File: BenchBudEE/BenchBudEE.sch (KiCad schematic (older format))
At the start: 0 parts

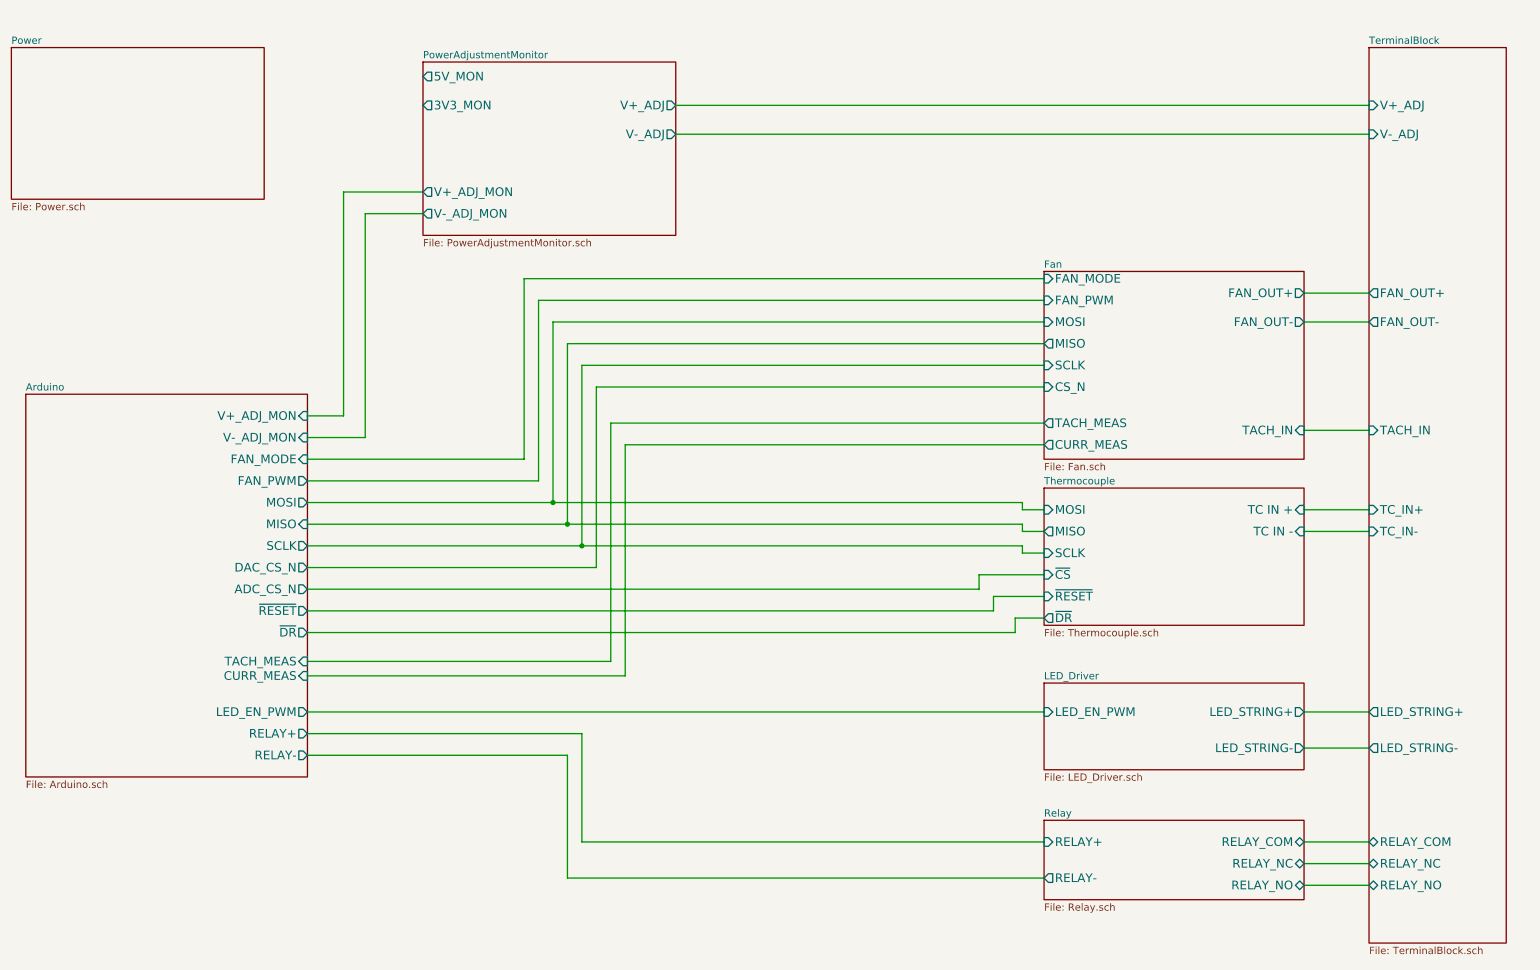
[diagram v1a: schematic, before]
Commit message: Associating the current/fan driver module components.
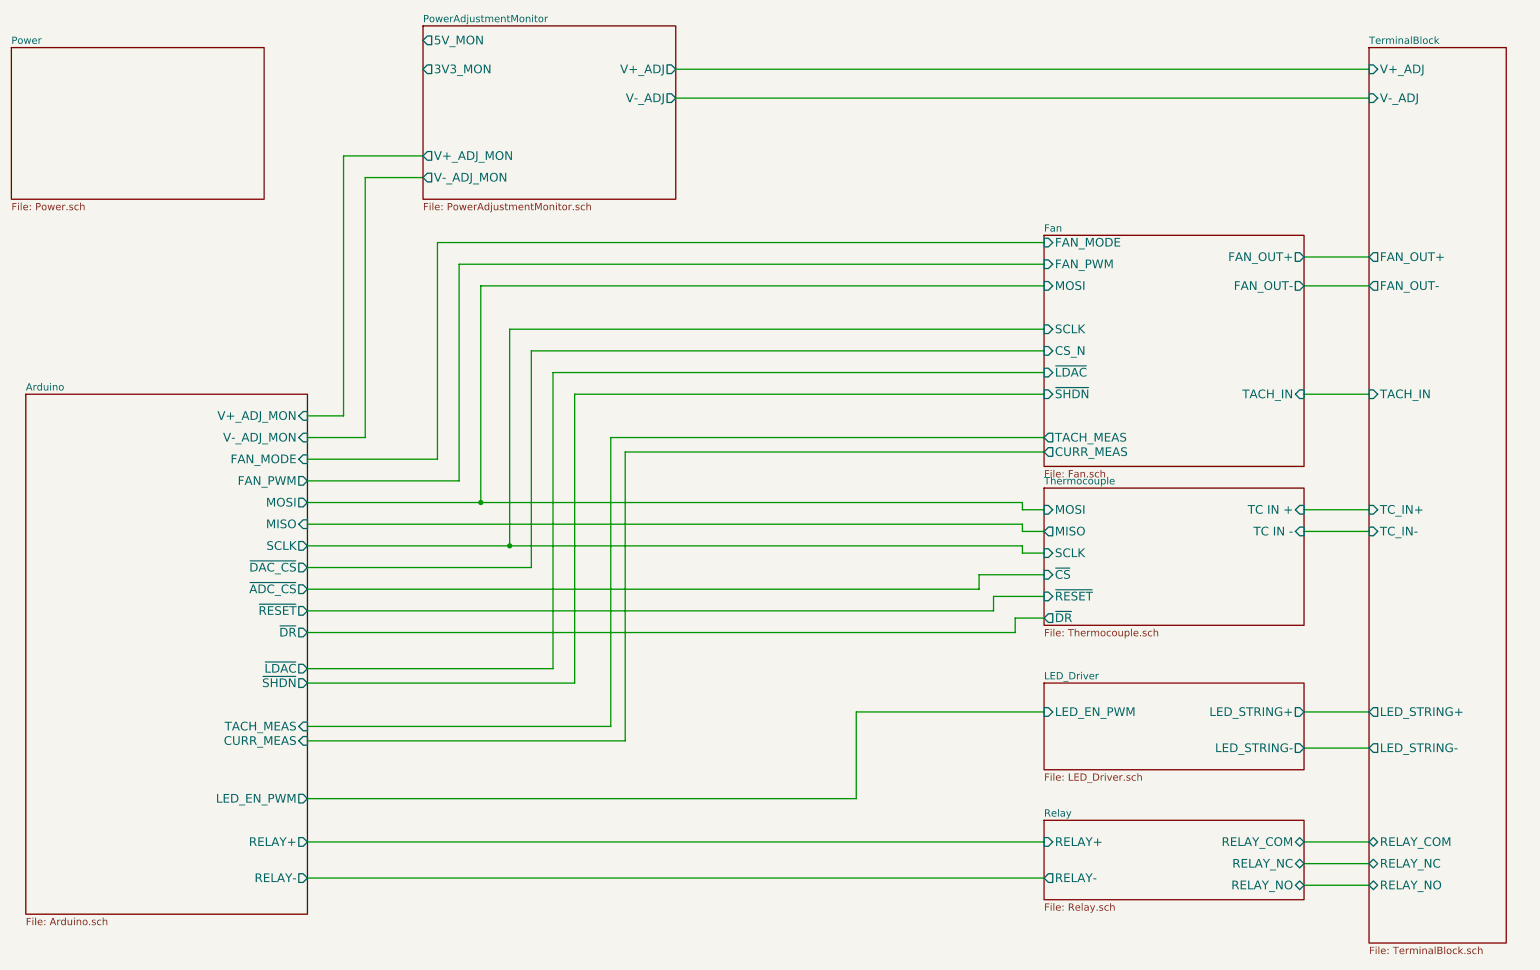
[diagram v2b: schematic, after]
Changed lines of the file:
@@
 $EndSheet
 $Sheet
-S 3550 850  1750 1200
+S 3550 600  1750 1200
 U 52F627C8
 F0 "PowerAdjustmentMonitor" 50
 F1 "PowerAdjustmentMonitor.sch" 50
-F2 "V+_ADJ" O R 5300 1150 60
-F3 "V-_ADJ" O R 5300 1350 60
-F4 "3V3_MON" O L 3550 1150 60
-F5 "5V_MON" O L 3550 950 60
-F6 "V+_ADJ_MON" O L 3550 1750 60
-F7 "V-_ADJ_MON" O L 3550 1900 60
-$EndSheet
-$Sheet
-S 7850 2300 1800 1300
+F2 "V+_ADJ" O R 5300 900 60
+F3 "V-_ADJ" O R 5300 1100 60
+F4 "3V3_MON" O L 3550 900 60
+F5 "5V_MON" O L 3550 700 60
+F6 "V+_ADJ_MON" O L 3550 1500 60
+F7 "V-_ADJ_MON" O L 3550 1650 60
+$EndSheet
+$Sheet
+S 7850 2050 1800 1600
 U 52EC4E13
 F0 "Fan" 50
 F1 "Fan.sch" 50
-F2 "MOSI" I L 7850 2650 60
-F3 "MISO" O L 7850 2800 60
-F4 "CS_N" I L 7850 3100 60
-F5 "SCLK" I L 7850 2950 60
-F6 "FAN_OUT+" O R 9650 2450 60
-F7 "TACH_IN" I R 9650 3400 60
-F8 "TACH_MEAS" O L 7850 3350 60
-F9 "CURR_MEAS" O L 7850 3500 60
-F10 "FAN_OUT-" O R 9650 2650 60
-F11 "FAN_PWM" I L 7850 2500 60
-F12 "FAN_MODE" I L 7850 2350 60
-$EndSheet
-Wire Wire Line
-	10100 1150 5300 1150
-Wire Wire Line
-	10100 1350 5300 1350
+F2 "MOSI" I L 7850 2400 60
+F3 "CS_N" I L 7850 2850 60
+F4 "SCLK" I L 7850 2700 60
+F5 "FAN_OUT+" O R 9650 2200 60
+F6 "TACH_IN" I R 9650 3150 60
+F7 "TACH_MEAS" O L 7850 3450 60
+F8 "CURR_MEAS" O L 7850 3550 60
+F9 "FAN_OUT-" O R 9650 2400 60
+F10 "FAN_PWM" I L 7850 2250 60
+F11 "FAN_MODE" I L 7850 2100 60
+F12 "~LDAC" I L 7850 3000 60
+F13 "~SHDN" I L 7850 3150 60
+$EndSheet
+Wire Wire Line
+	10100 900  5300 900
+Wire Wire Line
+	10100 1100 5300 1100
 $Sheet
 S 10100 750  950  6200
@@
 F0 "TerminalBlock" 50
 F1 "TerminalBlock.sch" 50
-F2 "V+_ADJ" I L 10100 1150 60
-F3 "V-_ADJ" I L 10100 1350 60
-F4 "FAN_OUT+" O L 10100 2450 60
-F5 "FAN_OUT-" O L 10100 2650 60
-F6 "TACH_IN" I L 10100 3400 60
+F2 "V+_ADJ" I L 10100 900 60
+F3 "V-_ADJ" I L 10100 1100 60
+F4 "FAN_OUT+" O L 10100 2200 60
+F5 "FAN_OUT-" O L 10100 2400 60
+F6 "TACH_IN" I L 10100 3150 60
 F7 "LED_STRING+" O L 10100 5350 60
 F8 "LED_STRING-" O L 10100 5600 60
@@
 $EndSheet
 Wire Wire Line
-	9650 2450 10100 2450
-Wire Wire Line
-	9650 2650 10100 2650
-Wire Wire Line
-	9650 3400 10100 3400
+	9650 2200 10100 2200
+Wire Wire Line
+	9650 2400 10100 2400
+Wire Wire Line
+	9650 3150 10100 3150
 Wire Wire Line
 	9650 6250 10100 6250
@@
 	2750 3300 3000 3300
 Wire Wire Line
-	3000 3300 3000 1750
-Wire Wire Line
-	3000 1750 3550 1750
-Wire Wire Line
-	2750 3450 3150 3450
-Wire Wire Line
-	3150 3450 3150 1900
-Wire Wire Line
-	3150 1900 3550 1900
-$Sheet
-S 800  3150 1950 2650
+	3000 3300 3000 1500
+Wire Wire Line
+	3150 3450 2750 3450
+Wire Wire Line
+	3150 1650 3150 3450
+$Sheet
+S 800  3150 1950 3600
 U 52EC4D59
 F0 "Arduino" 50
@@
 F3 "MISO" I R 2750 4050 60
 F4 "SCLK" O R 2750 4200 60
-F5 "TACH_MEAS" I R 2750 5000 60
-F6 "RELAY+" O R 2750 5500 60
-F7 "RELAY-" O R 2750 5650 60
-F8 "CURR_MEAS" I R 2750 5100 60
+F5 "TACH_MEAS" I R 2750 5450 60
+F6 "RELAY+" O R 2750 6250 60
+F7 "RELAY-" O R 2750 6500 60
+F8 "CURR_MEAS" I R 2750 5550 60
 F9 "V+_ADJ_MON" I R 2750 3300 60
 F10 "V-_ADJ_MON" I R 2750 3450 60
-F11 "LED_EN_PWM" O R 2750 5350 60
-F12 "DAC_CS_N" O R 2750 4350 60
-F13 "ADC_CS_N" O R 2750 4500 60
-F14 "FAN_PWM" O R 2750 3750 60
-F15 "FAN_MODE" I R 2750 3600 60
-F16 "~RESET" O R 2750 4650 60
-F17 "~DR" O R 2750 4800 60
-$EndSheet
-Wire Wire Line
-	2750 3750 4350 3750
+F11 "LED_EN_PWM" O R 2750 5950 60
+F12 "FAN_PWM" O R 2750 3750 60
+F13 "FAN_MODE" I R 2750 3600 60
+F14 "~RESET" O R 2750 4650 60
+F15 "~DR" O R 2750 4800 60
+F16 "~LDAC" O R 2750 5050 60
+F17 "~SHDN" O R 2750 5150 60
+F18 "~DAC_CS" O R 2750 4350 60
+F19 "~ADC_CS" O R 2750 4500 60
+$EndSheet
+Wire Wire Line
+	3800 3750 2750 3750
 Wire Wire Line
 	2750 3900 7700 3900
 Wire Wire Line
-	4450 3900 4450 2650
-Wire Wire Line
-	4450 2650 7850 2650
+	3950 2400 3950 3900
 Wire Wire Line
 	2750 4050 7700 4050
 Wire Wire Line
-	4550 4050 4550 2800
-Wire Wire Line
-	4550 2800 7850 2800
-Wire Wire Line
-	4850 3350 4850 5000
-Wire Wire Line
-	4850 3350 7850 3350
-Wire Wire Line
-	4950 3500 4950 5100
-Wire Wire Line
-	4950 3500 7850 3500
+	4850 3450 4850 5450
+Wire Wire Line
+	4950 3550 4950 5550
 Wire Wire Line
 	9650 3950 10100 3950
@@
 	9650 5600 10100 5600
 Wire Wire Line
-	7850 2950 4650 2950
-Wire Wire Line
-	4650 2950 4650 4200
+	4150 2700 4150 4200
 Wire Wire Line
 	2750 4200 7700 4200
 Wire Wire Line
-	2750 4350 4750 4350
-Wire Wire Line
-	4750 4350 4750 3100
-Wire Wire Line
-	4750 3100 7850 3100
-Connection ~ 4450 3900
-Connection ~ 4550 4050
-Connection ~ 4650 4200
+	4300 4350 2750 4350
+Wire Wire Line
+	4300 2850 4300 4350
+Connection ~ 3950 3900
+Connection ~ 4150 4200
 Wire Wire Line
 	7400 4500 2750 4500
 Wire Wire Line
-	2750 5350 7850 5350
-Wire Wire Line
-	2750 5650 4550 5650
-Wire Wire Line
-	4550 5650 4550 6500
-Wire Wire Line
-	4550 6500 7850 6500
-Wire Wire Line
-	2750 5500 4650 5500
-Wire Wire Line
-	4650 5500 4650 6250
-Wire Wire Line
-	4650 6250 7850 6250
+	2750 6500 7850 6500
+Wire Wire Line
+	2750 6250 7850 6250
 Wire Wire Line
 	9650 6400 10100 6400
@@
 	9650 6550 10100 6550
 Wire Wire Line
-	4350 3750 4350 2500
-Wire Wire Line
-	4350 2500 7850 2500
-Wire Wire Line
-	7850 2350 4250 2350
-Wire Wire Line
-	4250 2350 4250 3600
-Wire Wire Line
-	4250 3600 2750 3600
+	3800 2250 3800 3750
+Wire Wire Line
+	3650 2100 3650 3600
+Wire Wire Line
+	3650 3600 2750 3600
 Wire Wire Line
 	7700 3900 7700 3950
@@
 	7400 4400 7850 4400
 Wire Wire Line
-	4950 5100 2750 5100
-Wire Wire Line
-	4850 5000 2750 5000
-Wire Wire Line
 	2750 4650 7500 4650
 Wire Wire Line
@@
 Wire Wire Line
 	7650 4700 7850 4700
+Wire Wire Line
+	3000 1500 3550 1500
+Wire Wire Line
+	3150 1650 3550 1650
+Wire Wire Line
+	3650 2100 7850 2100
+Wire Wire Line
+	3800 2250 7850 2250
+Wire Wire Line
+	3950 2400 7850 2400
+Wire Wire Line
+	4150 2700 7850 2700
+Wire Wire Line
+	4300 2850 7850 2850
+Wire Wire Line
+	4950 3550 7850 3550
+Wire Wire Line
+	4850 3450 7850 3450
+Wire Wire Line
+	7850 5350 6550 5350
+Wire Wire Line
+	6550 5350 6550 5950
+Wire Wire Line
+	6550 5950 2750 5950
+Wire Wire Line
+	4950 5550 2750 5550
+Wire Wire Line
+	4850 5450 2750 5450
+Wire Wire Line
+	2750 5050 4450 5050
+Wire Wire Line
+	4450 5050 4450 3000
+Wire Wire Line
+	4450 3000 7850 3000
+Wire Wire Line
+	2750 5150 4600 5150
+Wire Wire Line
+	4600 5150 4600 3150
+Wire Wire Line
+	4600 3150 7850 3150
 $EndSCHEMATC
